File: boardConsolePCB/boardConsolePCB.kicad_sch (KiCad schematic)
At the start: 132 parts, among them J1 to HV cable, J2 SMA F, J3 PROG, J4 BUTTONS, J5 PWR, J6 FUEL/TRIM, J7 PRG_UART, Q1 BC548, Q2 IRML0030TR, Q3 IRML0030TR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

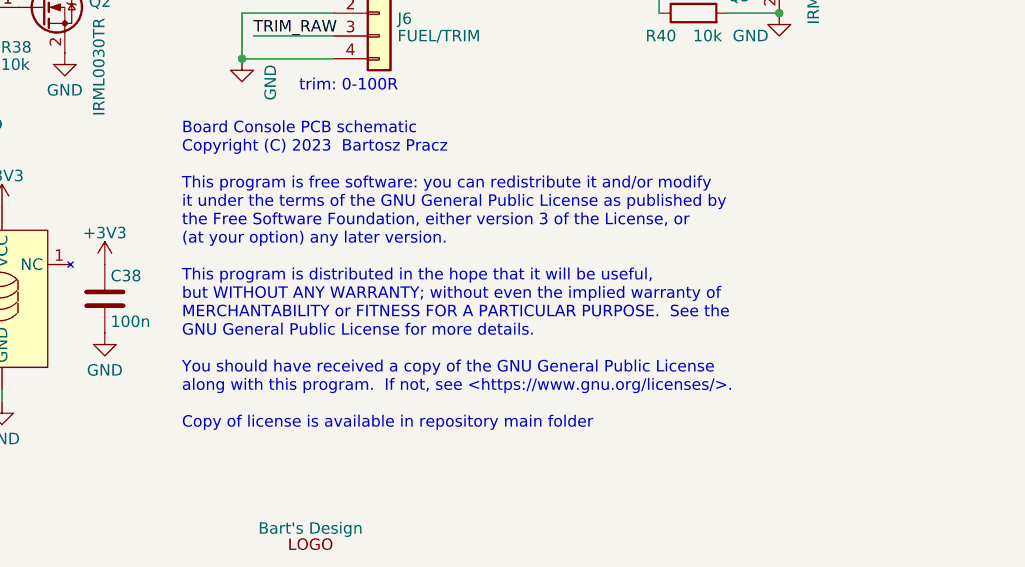
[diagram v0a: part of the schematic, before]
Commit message: added manu map
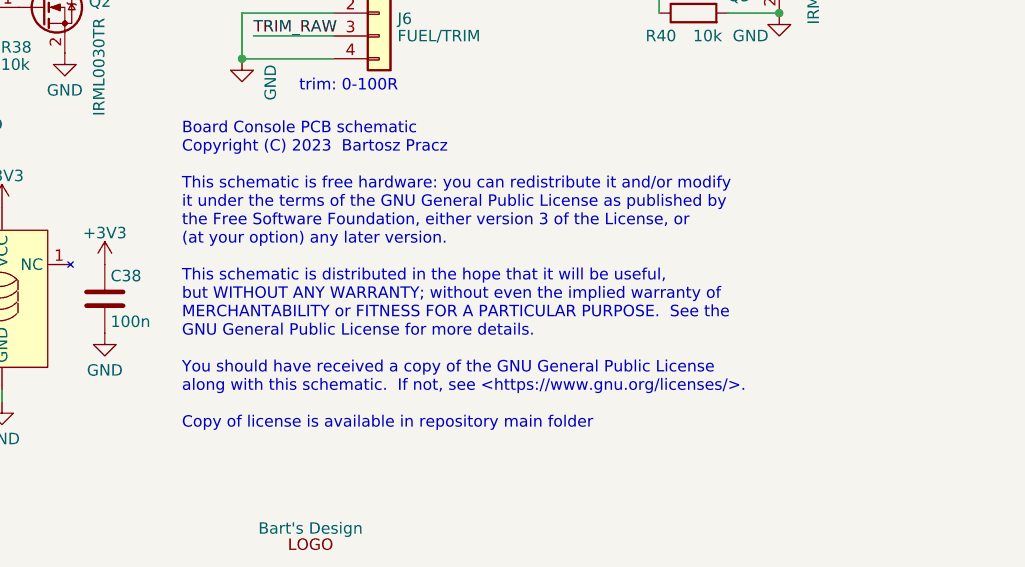
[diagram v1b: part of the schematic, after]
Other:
- note added: "Board Console PCB schematic Copyright (C) 2023 Bartosz Pracz This schematic is free hardware: you can redistribute it and/or modify it under the terms of the GNU General Public License as published by the Free Software Foundation, either version 3 of the License, or (at your option) any later version. This schematic is distributed in the hope that it will be useful, but WITHOUT ANY WARRANTY; with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"
- note removed: "Board Console PCB schematic Copyright (C) 2023 Bartosz Pracz This program is free software: you can redistribute it and/or modify it under the terms of the GNU General Public License as published by the Free Software Foundation, either version 3 of the License, or (at your option) any later version. This program is distributed in the hope that it will be useful, but WITHOUT ANY WARRANTY; without 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"
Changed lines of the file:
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@@
     (effects (font (size 1.27 1.27)) (justify left bottom))
   )
-  (text "	Board Console PCB schematic\n    Copyright (C) 2023  Bartosz Pracz\n\n    This program is free software: you can redistribute it and/or modify\n    it under the terms of the GNU General Public License as published by\n    the Free Software Foundation, either version 3 of the License, or\n    (at your option) any later version.\n\n    This program is distributed in the hope that it will be useful,\n    but WITHOUT ANY WARRANTY; without even the implied warranty of\n    MERCHANTABILITY or FITNESS FOR A PARTICULAR PURPOSE.  See the\n    GNU General Public License for more details.\n\n    You should have received a copy of the GNU General Public License\n    along with this program.  If not, see <https://www.gnu.org/licenses/>.\n\n    Copy of license is available in repository main folder"
+  (text "	Board Console PCB schematic\n    Copyright (C) 2023  Bartosz Pracz\n\n    This schematic is free hardware: you can redistribute it and/or modify\n    it under the terms of the GNU General Public License as published by\n    the Free Software Foundation, either version 3 of the License, or\n    (at your option) any later version.\n\n    This schematic is distributed in the hope that it will be useful,\n    but WITHOUT ANY WARRANTY; without even the implied warranty of\n    MERCHANTABILITY or FITNESS FOR A PARTICULAR PURPOSE.  See the\n    GNU General Public License for more details.\n\n    You should have received a copy of the GNU General Public License\n    along with this schematic.  If not, see <https://www.gnu.org/licenses/>.\n\n    Copy of license is available in repository main folder"
     (at 209.55 163.195 0)
     (effects (font (size 1.27 1.27)) (justify left bottom))

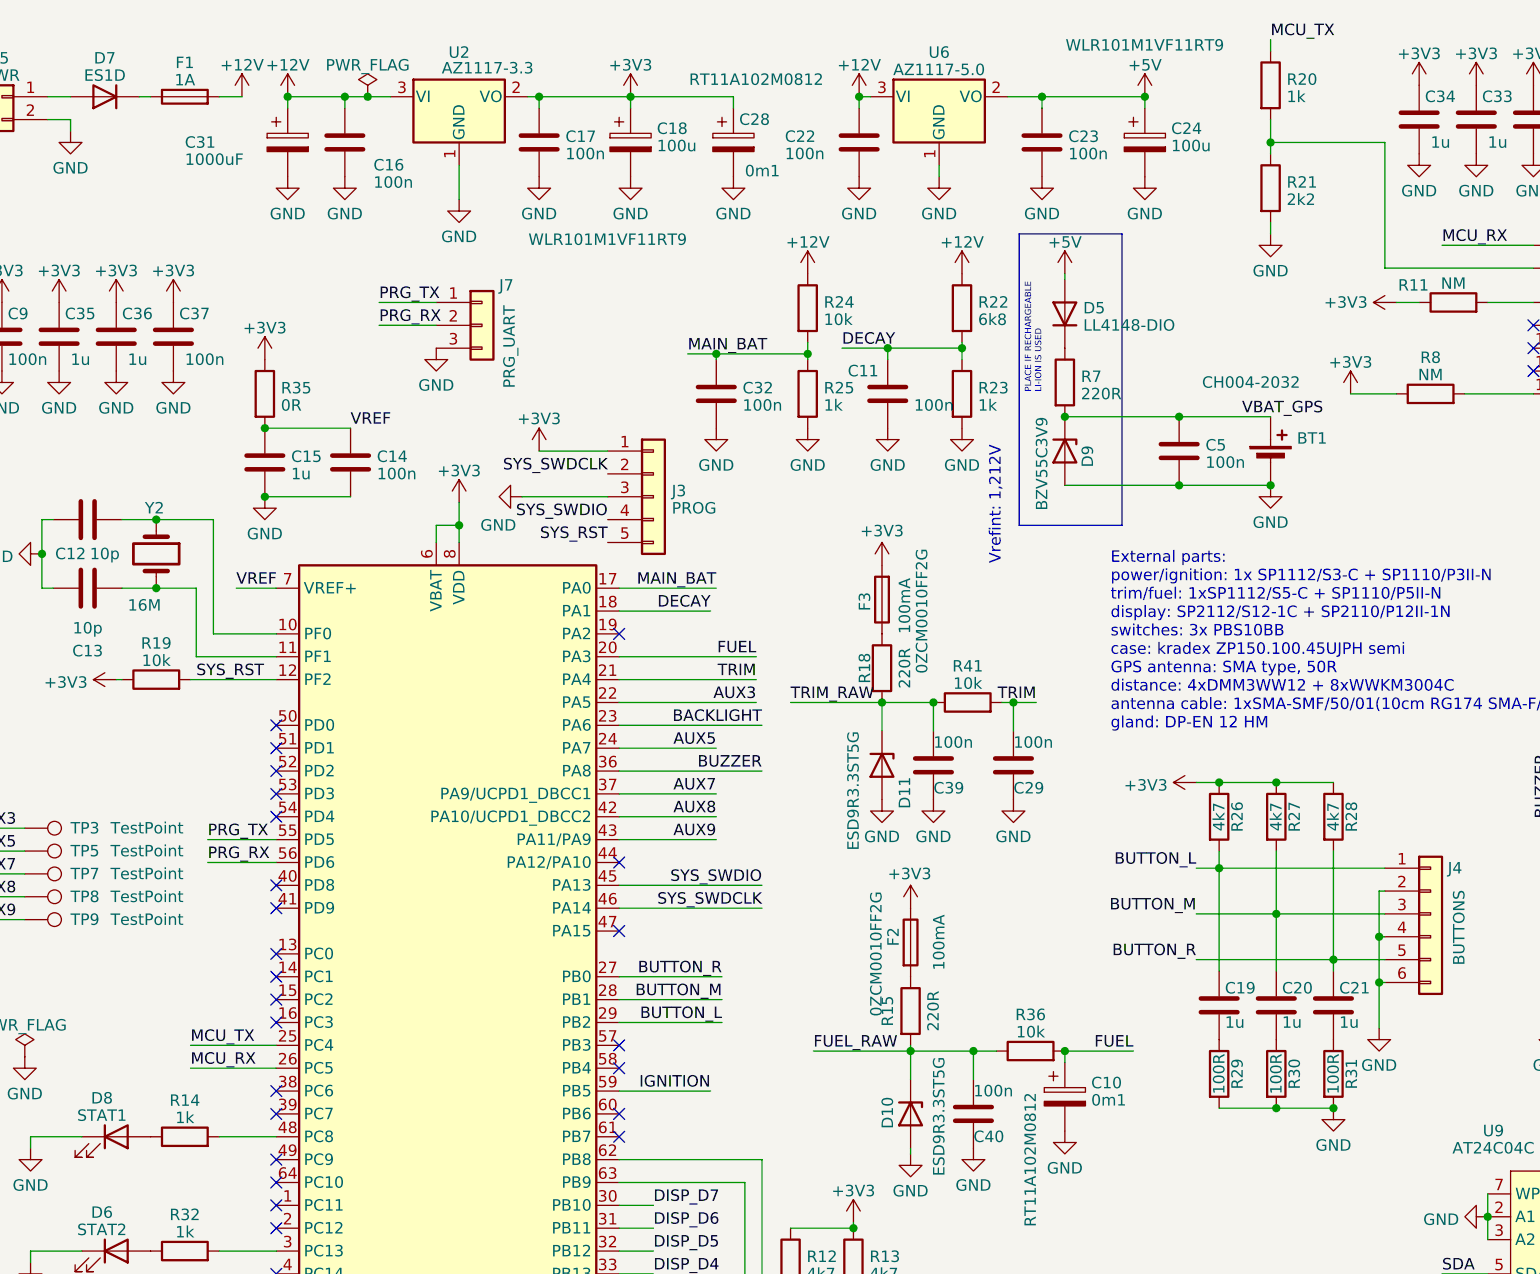
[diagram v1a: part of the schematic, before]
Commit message: correct values for polarized caps
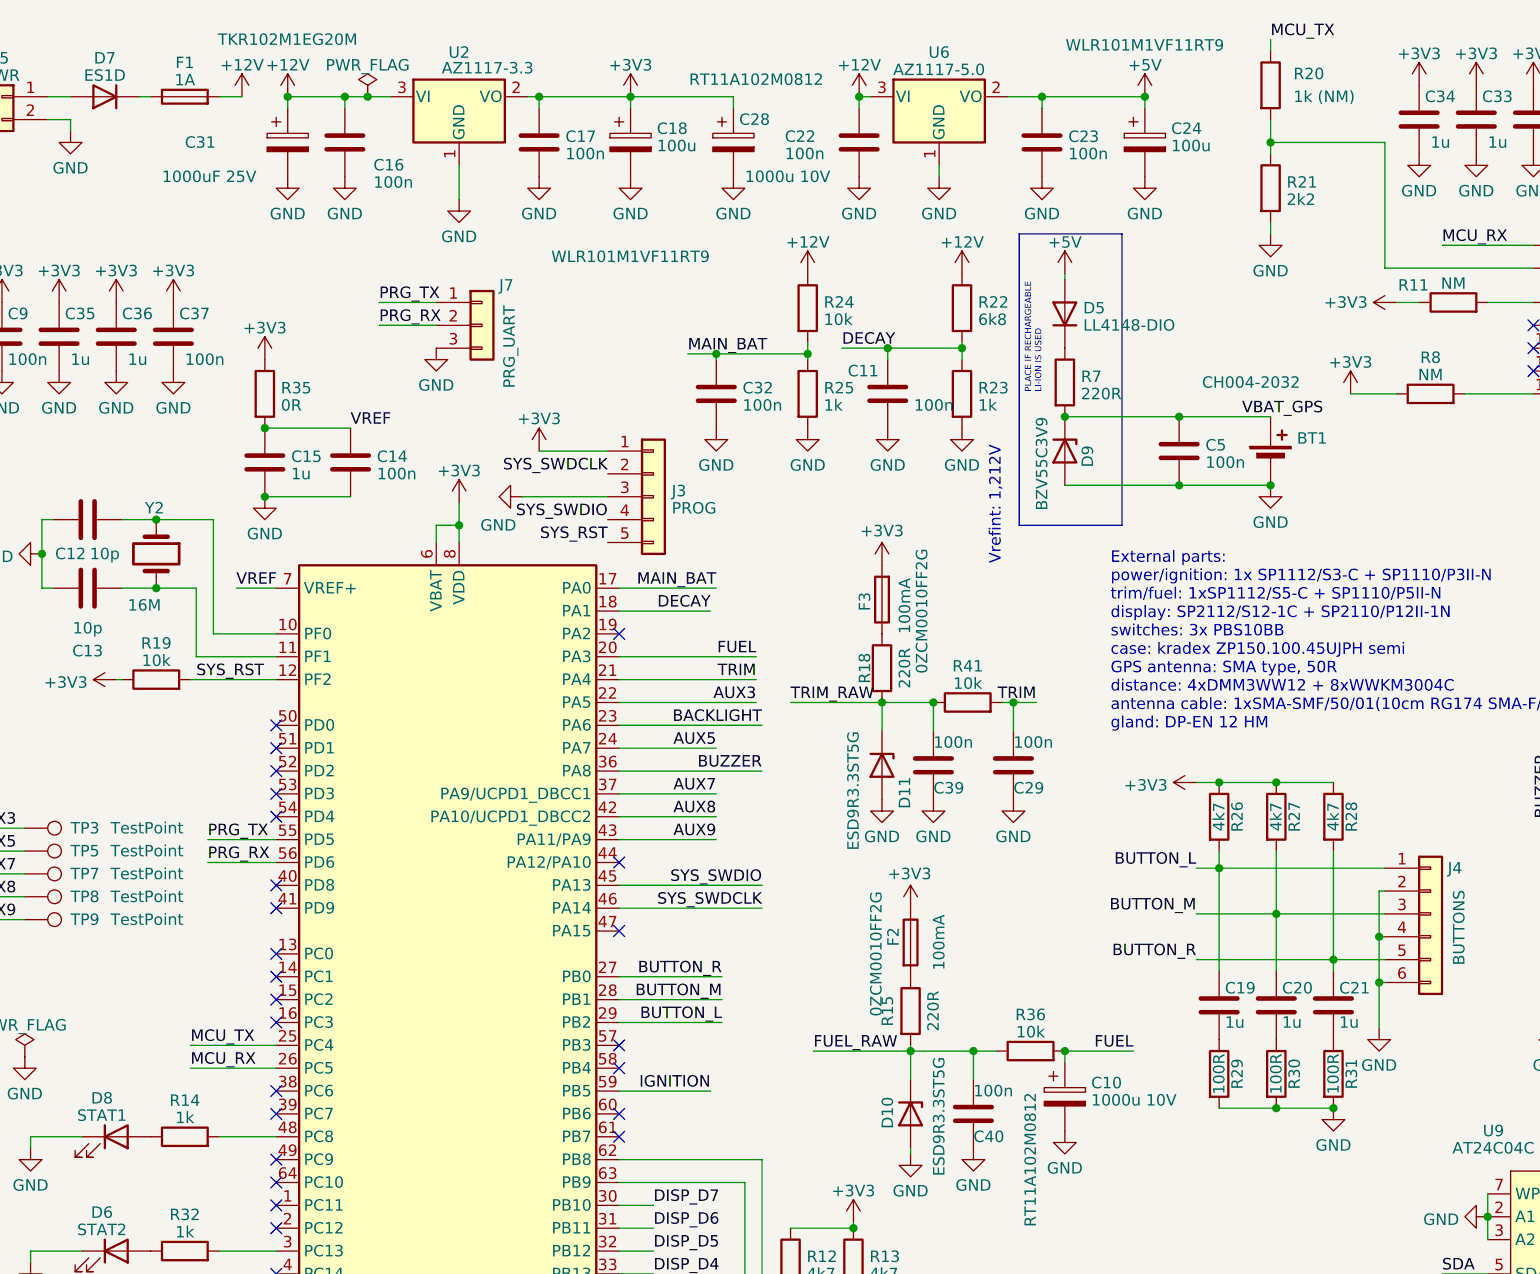
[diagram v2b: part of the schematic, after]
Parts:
- C10, C28: value 0m1 -> 1000u 10V
- C31: value 1000uF -> 1000uF 25V; Field4 (none) -> TKR102M1EG20M
- R20: value 1k -> 1k (NM)
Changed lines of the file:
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@@
       (effects (font (size 1.27 1.27)) (justify left))
     )
-    (property "Value" "0m1" (at 138.811 133.1033 0)
+    (property "Value" "1000u 10V" (at 138.811 133.1033 0)
       (effects (font (size 1.27 1.27)) (justify left))
     )
@@
       (effects (font (size 1.27 1.27)) (justify left))
     )
-    (property "Value" "1000uF" (at 38.1 28.575 0)
+    (property "Value" "1000uF 25V" (at 35.56 30.48 0)
       (effects (font (size 1.27 1.27)) (justify left))
     )
@@
       (effects (font (size 1.27 1.27)) hide)
     )
+    (property "Field4" "TKR102M1EG20M" (at 49.53 15.24 0)
+      (effects (font (size 1.27 1.27)))
+    )
     (pin "1")
     (pin "2")
@@
       (effects (font (size 1.27 1.27)) (justify left))
     )
-    (property "Value" "0m1" (at 100.33 29.845 0)
+    (property "Value" "1000u 10V" (at 100.33 30.48 0)
       (effects (font (size 1.27 1.27)) (justify left))
     )
@@
   (symbol (lib_id "Device:R") (at 158.75 20.32 0) (unit 1)
     (in_bom yes) (on_board yes) (dnp no) (fields_autoplaced)
-    (property "Reference" "R20" (at 160.528 19.6763 0)
+    (property "Reference" "R20" (at 161.29 19.05 0)
       (effects (font (size 1.27 1.27)) (justify left))
     )
-    (property "Value" "1k" (at 160.528 21.5973 0)
+    (property "Value" "1k (NM)" (at 161.29 21.59 0)
       (effects (font (size 1.27 1.27)) (justify left))
     )
@@
       (effects (font (size 1.27 1.27)) hide)
     )
-    (property "model" "WLR101M1VF11RT9" (at 85.09 37.465 0)
+    (property "model" "WLR101M1VF11RT9" (at 87.63 39.37 0)
       (effects (font (size 1.27 1.27)))
     )

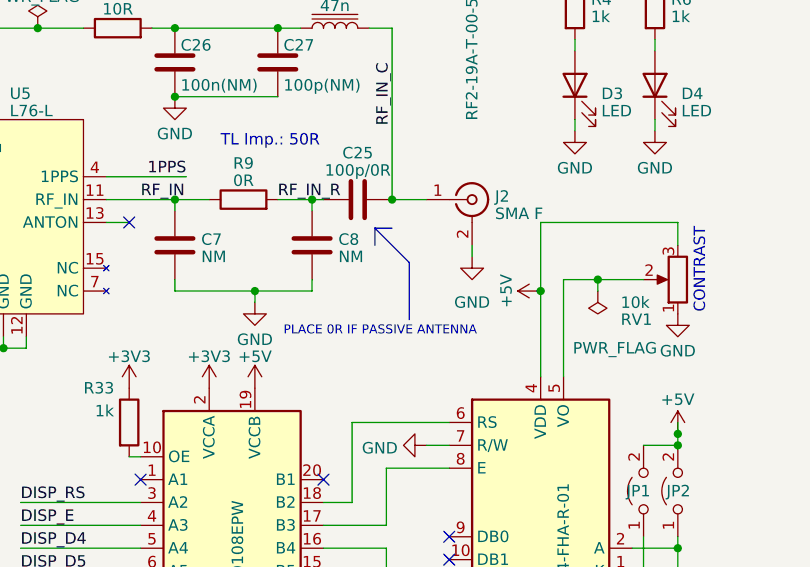
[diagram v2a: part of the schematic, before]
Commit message: correct description for antenna TL
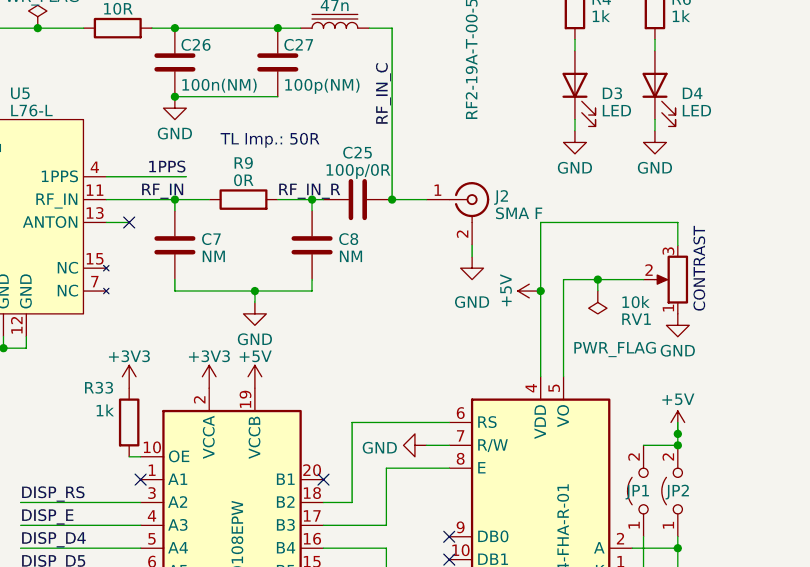
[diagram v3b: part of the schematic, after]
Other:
- note removed: "PLACE 0R IF PASSIVE ANTENNA"
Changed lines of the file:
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@@
-    (stroke (width 0) (type default))
-  )
-  (polyline (pts (xy 248.285 47.625) (xy 248.285 49.53))
     (stroke (width 0) (type default))
   )
@@
     (stroke (width 0) (type default))
   )
-  (polyline (pts (xy 248.285 47.625) (xy 252.095 51.435))
-    (stroke (width 0) (type default))
-  )
   (wire (pts (xy 241.3 54.61) (xy 241.3 53.34))
     (stroke (width 0) (type default))
@@
     (stroke (width 0) (type default))
   )
-  (polyline (pts (xy 248.285 47.625) (xy 250.19 47.625))
-    (stroke (width 0) (type default))
-  )
   (wire (pts (xy 226.06 54.61) (xy 226.06 53.34))
     (stroke (width 0) (type default))
@@
   )
   (wire (pts (xy 266.7 46.99) (xy 281.94 46.99))
-    (stroke (width 0) (type default))
-  )
-  (polyline (pts (xy 252.095 51.435) (xy 252.095 57.785))
     (stroke (width 0) (type default))
   )
@@
     (effects (font (size 0.7 0.7)) (justify left bottom))
   )
-  (text "PLACE 0R IF PASSIVE ANTENNA" (at 238.125 59.69 0)
-    (effects (font (size 1 1)) (justify left bottom))
-  )
   (text "CONTRAST" (at 285.115 57.15 90)
